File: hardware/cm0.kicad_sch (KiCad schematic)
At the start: 0 parts

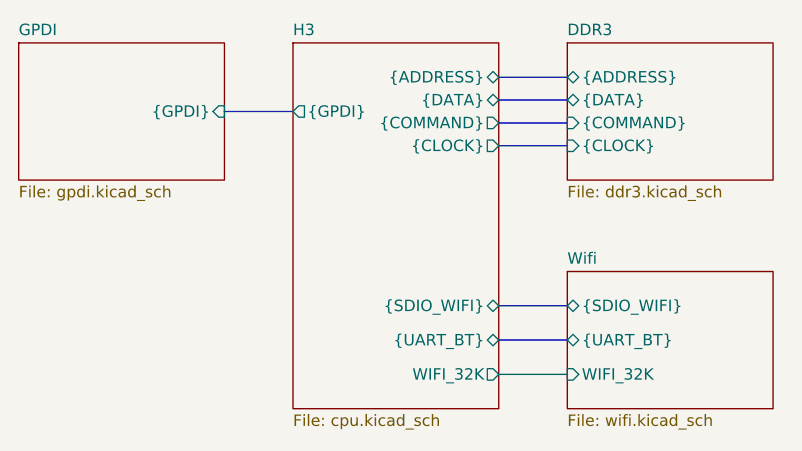
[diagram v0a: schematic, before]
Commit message: Re-routed DDR3 on L4 & drew USB schematic
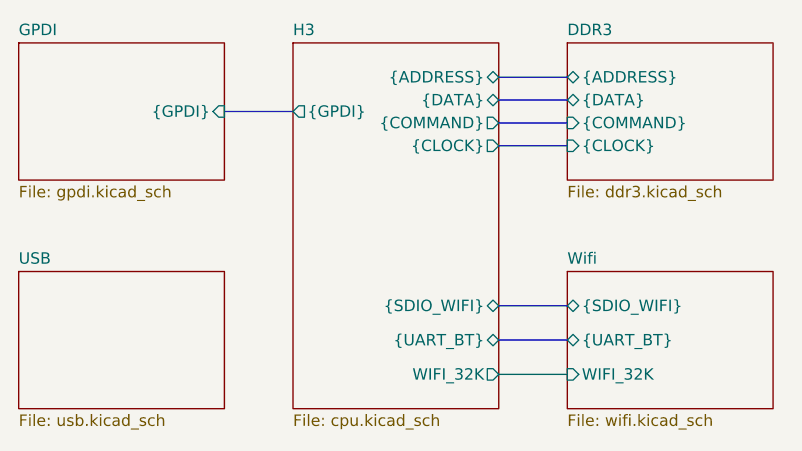
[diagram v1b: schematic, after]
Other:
- added sheet USB (usb.kicad_sch)
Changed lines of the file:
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@@
+	)
+	(sheet
+		(at 71.12 58.42)
+		(size 22.86 15.24)
+		(exclude_from_sim no)
+		(in_bom yes)
+		(on_board yes)
+		(dnp no)
+		(fields_autoplaced yes)
+		(stroke
+			(width 0.1524)
+			(type solid)
+		)
+		(fill
+			(color 0 0 0 0.0000)
+		)
+		(property "Sheetname" "USB"
+			(at 71.12 57.7084 0)
+			(effects
+				(font
+					(size 1.27 1.27)
+				)
+				(justify left bottom)
+			)
+		)
+		(property "Sheetfile" "usb.kicad_sch"
+			(at 71.12 74.2446 0)
+			(effects
+				(font
+					(size 1.27 1.27)
+				)
+				(justify left top)
+			)
+		)
+		(instances
+			(project "cm0"
+				(path "/b53f5dbb-8078-4818-9e8f-fdf90ba6d854"
+					(page "6")
+				)
+			)
+		)
 	)
 	(sheet
